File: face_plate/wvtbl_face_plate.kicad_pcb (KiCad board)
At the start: 2 copper layers, 30 x 128.5 mm, 10 parts, among them U1 WVTBL

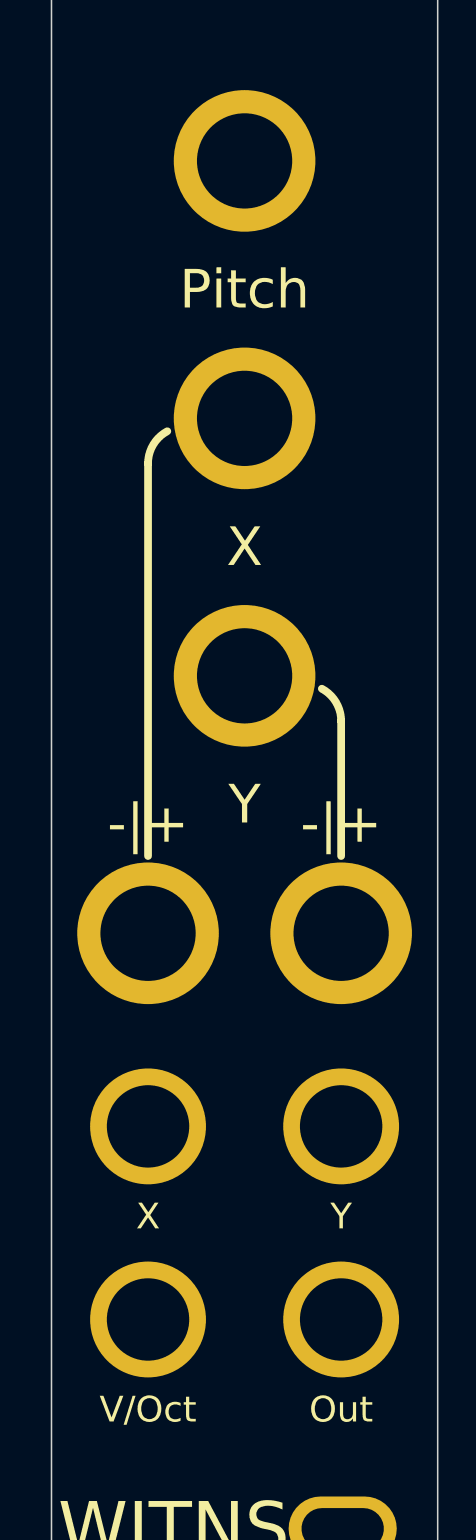
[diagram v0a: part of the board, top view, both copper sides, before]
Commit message: Corrections on faceplate holes place and sizes
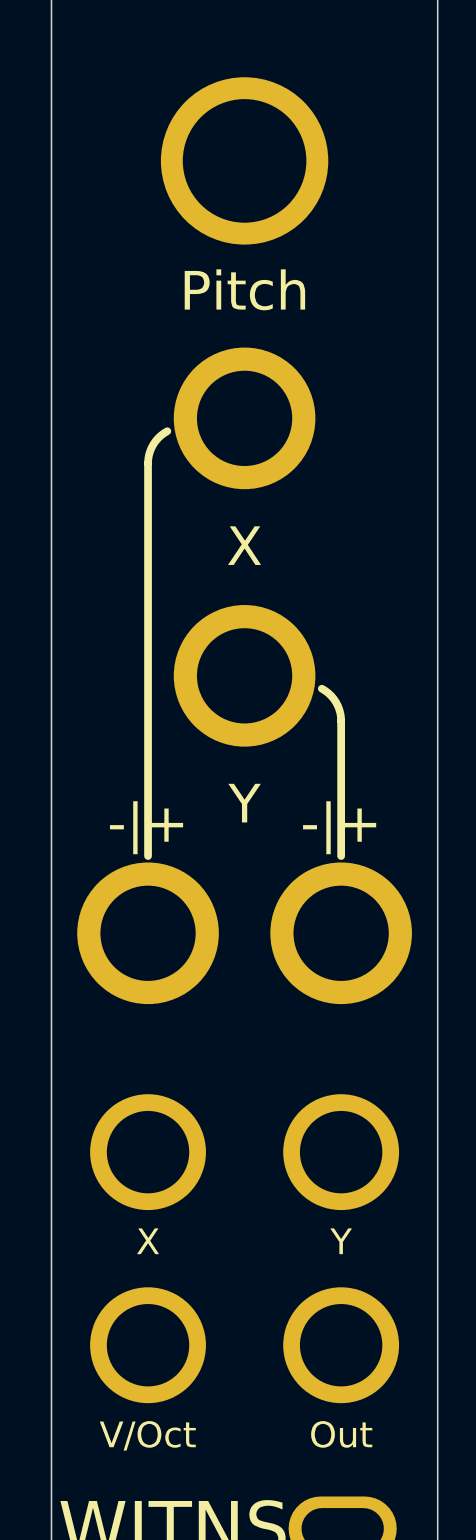
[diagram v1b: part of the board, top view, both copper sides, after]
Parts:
- H101: footprint WITNS:PotentiometerHole_7.4mm_M7_Pad -> WITNS:EncoderHole_9.4mm_M9_Pad
- moved H102 2.00 mm to (42.5, 147.0)
- moved H104 2.00 mm to (42.5, 132.0)
- moved H106 2.00 mm to (57.5, 132.0)
- moved H108 2.00 mm to (57.5, 147.0)
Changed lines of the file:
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@@
   )
   (footprint "WITNS:Thonkiconn_6.4mm_M6_Pad" (layer "F.Cu")
-    (at 42.5 130)
+    (at 42.5 132)
     (descr "Mounting Hole 6.4mm, M6")
     (tags "mounting hole 6.4mm m6")
@@
   )
   (footprint "WITNS:Thonkiconn_6.4mm_M6_Pad" (layer "F.Cu")
-    (at 57.5 130)
+    (at 57.5 132)
     (descr "Mounting Hole 6.4mm, M6")
     (tags "mounting hole 6.4mm m6")
@@
   )
   (footprint "WITNS:Thonkiconn_6.4mm_M6_Pad" (layer "F.Cu")
-    (at 57.5 145)
+    (at 57.5 147)
     (descr "Mounting Hole 6.4mm, M6")
     (tags "mounting hole 6.4mm m6")
@@
       (net 1 "GND") (pinfunction "1") (pintype "input"))
   )
-  (footprint "WITNS:PotentiometerHole_7.4mm_M7_Pad" (layer "F.Cu")
+  (footprint "WITNS:EncoderHole_9.4mm_M9_Pad" (layer "F.Cu")
     (at 50 55)
     (descr "Mounting Hole 6.4mm, M6")
@@
       (effects (font (size 1 1) (thickness 0.15)))
     )
-    (fp_text value "Pitch" (at 0 10) (layer "F.SilkS")
+    (fp_text value "Pitch" (at 0 10.16) (layer "F.SilkS")
       (effects (font (size 3 3) (thickness 0.45)))
     )
@@
     (fp_circle (center 0 0) (end 5.55 0) (layer "Cmts.User") (width 0.15) (fill none))
     (fp_circle (center 0 0) (end 5.6 0) (layer "F.CrtYd") (width 0.05) (fill none))
-    (pad "1" thru_hole circle (at 0 0) (size 11 11) (drill 7.4) (layers *.Cu *.Mask)
+    (pad "1" thru_hole circle (at 0 0) (size 13 13) (drill 9.6) (layers *.Cu *.Mask)
       (net 1 "GND") (pinfunction "1") (pintype "input"))
   )
   (footprint "WITNS:Thonkiconn_6.4mm_M6_Pad" (layer "F.Cu")
-    (at 42.5 145)
+    (at 42.5 147)
     (descr "Mounting Hole 6.4mm, M6")
     (tags "mounting hole 6.4mm m6")
